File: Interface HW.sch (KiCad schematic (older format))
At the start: 35 parts

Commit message: Still working
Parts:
- removed C? (x3): 0.1uF, ~, symbol CSMALL
- removed J? (x4): CONN_8, ~, symbol CONN_8
- removed R? (x18): R_US, symbol R_US
- removed TP?: TEST, symbol CONNECTOR
- removed U? (x2): DACX311, symbol DACX311
- removed U? (x5): OPA237, symbol OPA237
- removed U? (x2): 74XXX1G32, symbol 74XXX1G32
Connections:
- net labels removed: +15V, -15V, 3V3, ADC_A0, ADC_A1, ADC_A2, ADC_A4, ADC_A5, ADC_A6, ADC_B0, ADC_B1, ADC_B2, ADC_B4, ADC_B6, DAC_X+, DAC_X-, DAC_Y+, DAC_Y-, EPWM_1A, EPWM_1A_DAC, EPWM_1B, EPWM_2A, EPWM_2B, EPWM_3A, EPWM_3B, EPWM_4A, EPWM_4B, GND, GPIO_12, GPIO_34, SCL_A, SDA_A, SPICLK_A, SPISIMO_A, SPISOMI_A, SPISTE_A
- wire segments 154 -> 0
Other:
- note removed: "SCL SDA USED AS GPIO"

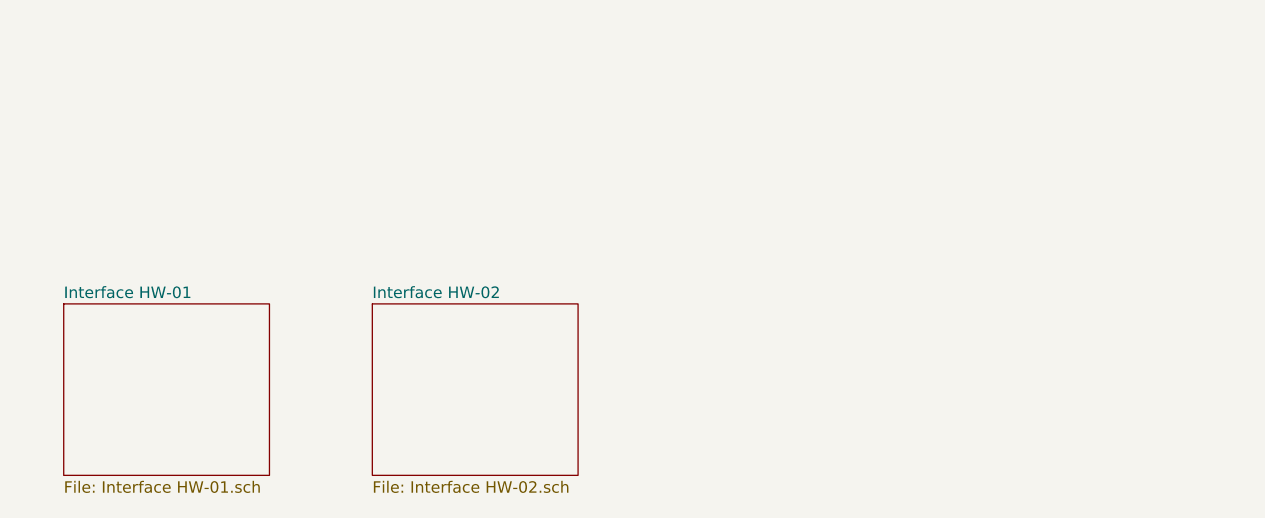
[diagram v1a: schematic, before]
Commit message: added new page for Y axis
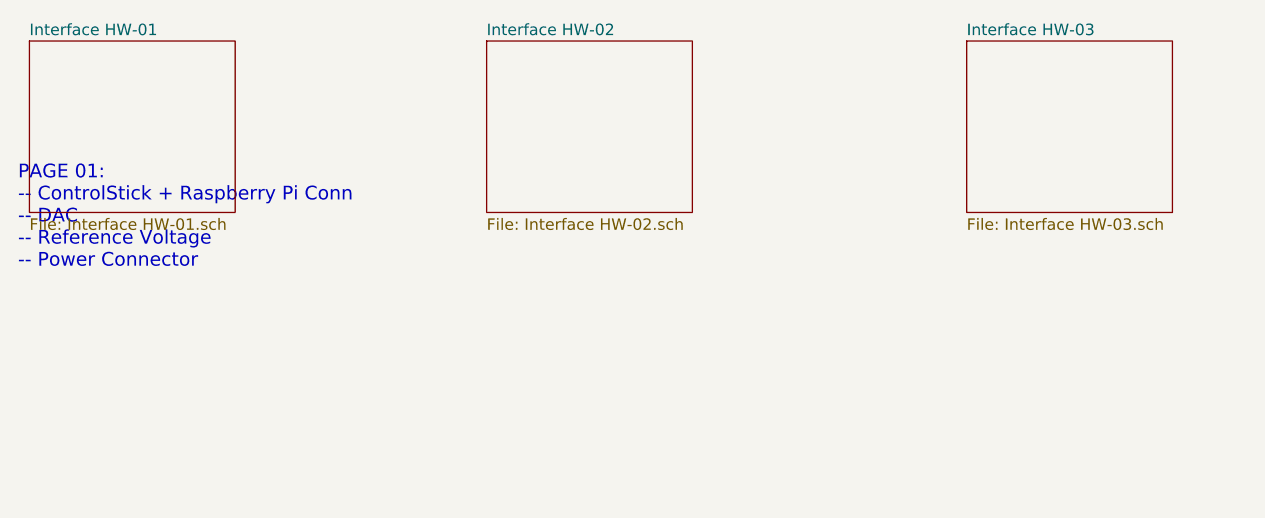
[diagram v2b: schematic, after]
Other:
- note added: "PAGE 01:\n-- ControlStick + Raspberry Pi Conn\n-- DAC\n-- Reference Voltage\n-- Power Connector\n"
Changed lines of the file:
@@
 $Descr A 11000 8500
 encoding utf-8
-Sheet 1 3
+Sheet 1 4
 Title "Defcon Bot Interface Brd"
 Date "2 apr 2014"
@@
 $EndDescr
 $Sheet
-S 950  6950 900  750
+S 800  5800 900  750
 U 533B4F18
 F0 "Interface HW-01" 50
@@
 $EndSheet
 $Sheet
-S 2300 6950 900  750
+S 2800 5800 900  750
 U 533B5168
 F0 "Interface HW-02" 50
@@
 EndData
 $EndBitmap
+$Sheet
+S 4900 5800 900  750
+U 533B7211
+F0 "Interface HW-03" 50
+F1 "Interface HW-03.sch" 50
+$EndSheet
+Text Notes 750  6800 0    60   ~ 0
+PAGE 01:\n-- ControlStick + Raspberry Pi Conn\n-- DAC\n-- Reference Voltage\n-- Power Connector\n
 $EndSCHEMATC

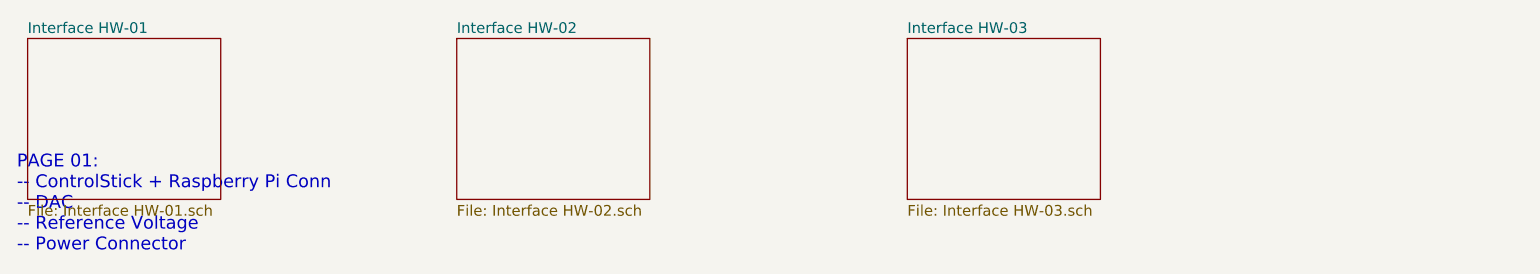
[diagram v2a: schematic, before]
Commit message: Modified schematic, added laser driver and page for buck converter
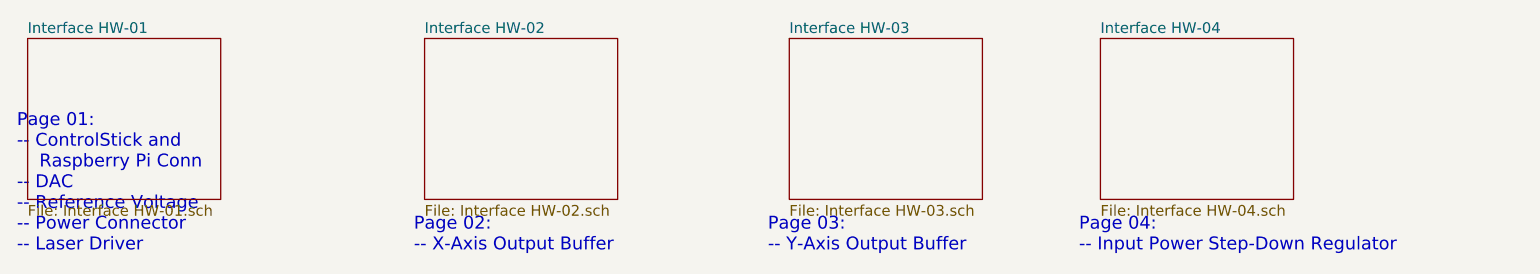
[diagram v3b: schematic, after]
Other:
- note added: "Page 01:\n-- ControlStick and \n Raspberry Pi Conn\n-- DAC\n-- Reference Voltage\n-- Power Connector\n-- Laser Driver\n"
- note added: "Page 02:\n-- X-Axis Output Buffer\n"
- note added: "Page 03:\n-- Y-Axis Output Buffer\n"
- note added: "Page 04:\n-- Input Power Step-Down Regulator\n"
- note removed: "PAGE 01:\n-- ControlStick + Raspberry Pi Conn\n-- DAC\n-- Reference Voltage\n-- Power Connector\n"
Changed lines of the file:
@@
 $Descr A 11000 8500
 encoding utf-8
-Sheet 1 4
+Sheet 1 5
 Title "Defcon Bot Interface Brd"
-Date "2 apr 2014"
+Date "5 apr 2014"
 Rev "1"
 Comp ""
@@
 $EndSheet
 $Sheet
-S 2800 5800 900  750
+S 2650 5800 900  750
 U 533B5168
 F0 "Interface HW-02" 50
@@
 $EndBitmap
 $Sheet
-S 4900 5800 900  750
+S 4350 5800 900  750
 U 533B7211
 F0 "Interface HW-03" 50
@@
 $EndSheet
 Text Notes 750  6800 0    60   ~ 0
-PAGE 01:\n-- ControlStick + Raspberry Pi Conn\n-- DAC\n-- Reference Voltage\n-- Power Connector\n
+Page 01:\n-- ControlStick and \n    Raspberry Pi Conn\n-- DAC\n-- Reference Voltage\n-- Power Connector\n-- Laser Driver\n
+Text Notes 2600 6800 0    60   ~ 0
+Page 02:\n-- X-Axis Output Buffer\n
+Text Notes 4250 6800 0    60   ~ 0
+Page 03:\n-- Y-Axis Output Buffer\n
+$Sheet
+S 5800 5800 900  750
+U 53404437
+F0 "Interface HW-04" 50
+F1 "Interface HW-04.sch" 50
+$EndSheet
+Text Notes 5700 6800 0    60   ~ 0
+Page 04:\n-- Input Power Step-Down Regulator\n
 $EndSCHEMATC
